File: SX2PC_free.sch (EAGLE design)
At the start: 5 parts

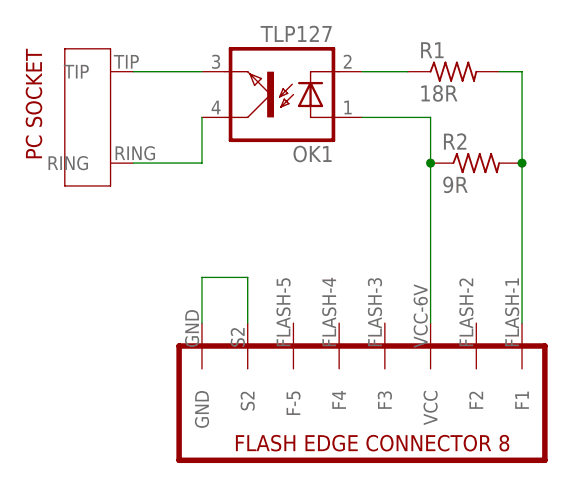
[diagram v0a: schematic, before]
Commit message: Build a prototype and checked operation. Now working. Version 2.0
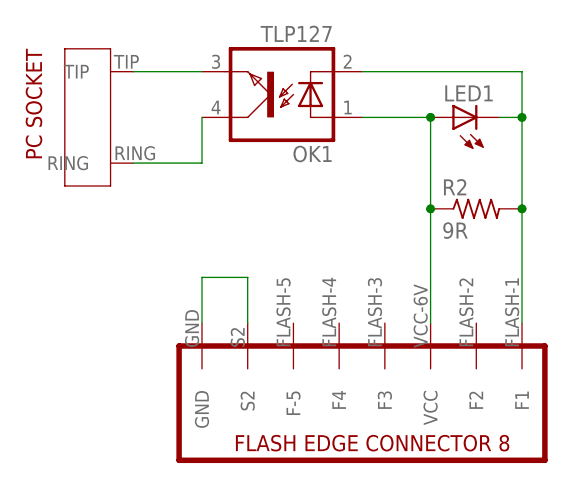
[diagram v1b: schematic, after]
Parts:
- removed R1: 18R, rcl:R-US_R0603
- added LED1: (no value), led:LEDCHIP-LED0805
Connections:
- removed net N$2: OK1.C, R1.1
- net GND: now also LED1.C, OK1.C; no longer R1.2
- net N$3: now also LED1.A
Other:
- moved on the sheet: R2
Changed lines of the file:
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@@
 <part name="U$1" library="openSX70" deviceset="SX70-FLASH-EDGE8-MALE" device=""/>
 <part name="U$2" library="openSX70" deviceset="PC-SOCKET-KAISER-1311" device=""/>
-<part name="R1" library="rcl" library_urn="urn:adsk.eagle:library:334" deviceset="R-US_" device="R0603" package3d_urn="urn:adsk.eagle:package:23555/2" value="18R"/>
 <part name="OK1" library="openSX70" deviceset="TLP127" device=""/>
 <part name="R2" library="rcl" library_urn="urn:adsk.eagle:library:334" deviceset="R-US_" device="R0603" package3d_urn="urn:adsk.eagle:package:23555/2" value="9R"/>
+<part name="LED1" library="led" library_urn="urn:adsk.eagle:library:259" deviceset="LED" device="CHIP-LED0805" package3d_urn="urn:adsk.eagle:package:15818/1"/>
 </parts>
 <sheets>
@@
 <instance part="U$1" gate="G$1" x="99.06" y="15.24"/>
 <instance part="U$2" gate="G$1" x="12.7" y="55.88" rot="MR270"/>
-<instance part="R1" gate="G$1" x="53.34" y="60.96"/>
 <instance part="OK1" gate="G$1" x="33.02" y="58.42" rot="R180"/>
-<instance part="R2" gate="G$1" x="55.88" y="50.8"/>
+<instance part="R2" gate="G$1" x="55.88" y="45.72"/>
+<instance part="LED1" gate="G$1" x="53.34" y="55.88" rot="R90"/>
 </instances>
 <busses>
@@
 </segment>
 </net>
-<net name="N$2" class="0">
-<segment>
-<pinref part="OK1" gate="G$1" pin="C"/>
-<pinref part="R1" gate="G$1" pin="1"/>
-<wire x1="43.18" y1="60.96" x2="48.26" y2="60.96" width="0.1524" layer="91"/>
-</segment>
-</net>
 <net name="GND" class="0">
 <segment>
-<pinref part="R1" gate="G$1" pin="2"/>
 <pinref part="U$1" gate="G$1" pin="F1"/>
-<wire x1="58.42" y1="60.96" x2="60.96" y2="60.96" width="0.1524" layer="91"/>
-<wire x1="60.96" y1="60.96" x2="60.96" y2="50.8" width="0.1524" layer="91"/>
-<wire x1="60.96" y1="50.8" x2="60.96" y2="33.02" width="0.1524" layer="91"/>
+<wire x1="60.96" y1="60.96" x2="60.96" y2="55.88" width="0.1524" layer="91"/>
+<wire x1="60.96" y1="55.88" x2="60.96" y2="45.72" width="0.1524" layer="91"/>
+<wire x1="60.96" y1="45.72" x2="60.96" y2="33.02" width="0.1524" layer="91"/>
 <pinref part="R2" gate="G$1" pin="2"/>
-<junction x="60.96" y="50.8"/>
+<junction x="60.96" y="45.72"/>
+<pinref part="OK1" gate="G$1" pin="C"/>
+<wire x1="43.18" y1="60.96" x2="60.96" y2="60.96" width="0.1524" layer="91"/>
+<pinref part="LED1" gate="G$1" pin="C"/>
+<wire x1="58.42" y1="55.88" x2="60.96" y2="55.88" width="0.1524" layer="91"/>
+<junction x="60.96" y="55.88"/>
 </segment>
 </net>
@@
 <wire x1="50.8" y1="55.88" x2="43.18" y2="55.88" width="0.1524" layer="91"/>
 <pinref part="R2" gate="G$1" pin="1"/>
-<wire x1="50.8" y1="50.8" x2="50.8" y2="55.88" width="0.1524" layer="91"/>
-<junction x="50.8" y="50.8"/>
+<wire x1="50.8" y1="45.72" x2="50.8" y2="55.88" width="0.1524" layer="91"/>
+<junction x="50.8" y="45.72"/>
 <pinref part="U$1" gate="G$1" pin="VCC"/>
-<wire x1="50.8" y1="33.02" x2="50.8" y2="50.8" width="0.1524" layer="91"/>
+<wire x1="50.8" y1="33.02" x2="50.8" y2="45.72" width="0.1524" layer="91"/>
+<pinref part="LED1" gate="G$1" pin="A"/>
+<junction x="50.8" y="55.88"/>
 </segment>
 </net>

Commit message: Connected F1 and F5 to VCC or it doesn't work!
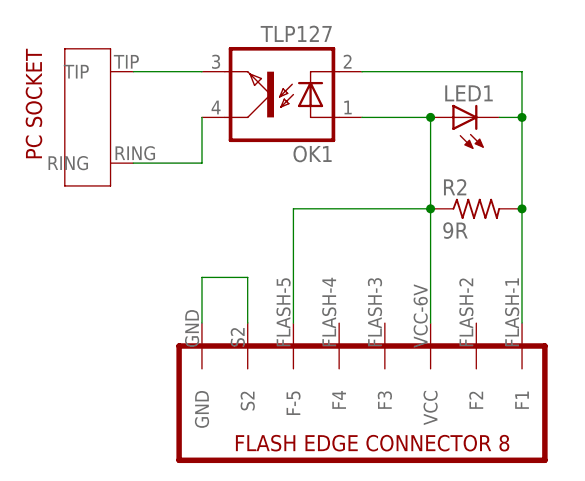
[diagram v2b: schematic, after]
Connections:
- net N$3: now also U$1.F-5
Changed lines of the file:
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@@
 <pinref part="LED1" gate="G$1" pin="A"/>
 <junction x="50.8" y="55.88"/>
+<pinref part="U$1" gate="G$1" pin="F-5"/>
+<wire x1="35.56" y1="33.02" x2="35.56" y2="45.72" width="0.1524" layer="91"/>
+<wire x1="35.56" y1="45.72" x2="50.8" y2="45.72" width="0.1524" layer="91"/>
 </segment>
 </net>
